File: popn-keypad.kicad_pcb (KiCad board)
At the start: 2 copper layers, 10 parts, among them U1 Arduino_Pro_Micro

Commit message: Defined edge cuts, added filled zones
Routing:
- added copper zone on B.Cu, net (none)
- added copper zone on F.Cu, net (none)
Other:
- board outline added: 123.8 x 38.1 mm
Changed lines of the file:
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@@
 		)
+	)
+	(gr_rect
+		(start 95.2 66.64)
+		(end 218.96 104.72)
+		(stroke
+			(width 0.05)
+			(type default)
+		)
+		(fill no)
+		(layer "Edge.Cuts")
 	)
 	(segment
@@
 		(net 10)
 	)
+	(zone
+		(net 0)
+		(net_name "")
+		(layers "F.Cu" "B.Cu")
+		(hatch edge 0.5)
+		(connect_pads
+			(clearance 0.5)
+		)
+		(min_thickness 0.25)
+		(filled_areas_thickness no)
+		(fill yes
+			(thermal_gap 0.5)
+			(thermal_bridge_width 0.5)
+			(island_removal_mode 1)
+			(island_area_min 10)
+		)
+		(polygon
+			(pts
+				(xy 85.68 57.12) (xy 228.48 57.12) (xy 228.48 114.24) (xy 85.68 114.24)
+			)
+		)
+	)
 	(embedded_fonts no)

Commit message: Hotfix
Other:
- board size 123.8 x 38.1 mm -> 119 x 42.8 mm
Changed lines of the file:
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@@
 	)
 	(gr_rect
-		(start 95.2 66.64)
+		(start 99.96 61.88)
 		(end 218.96 104.72)
 		(stroke

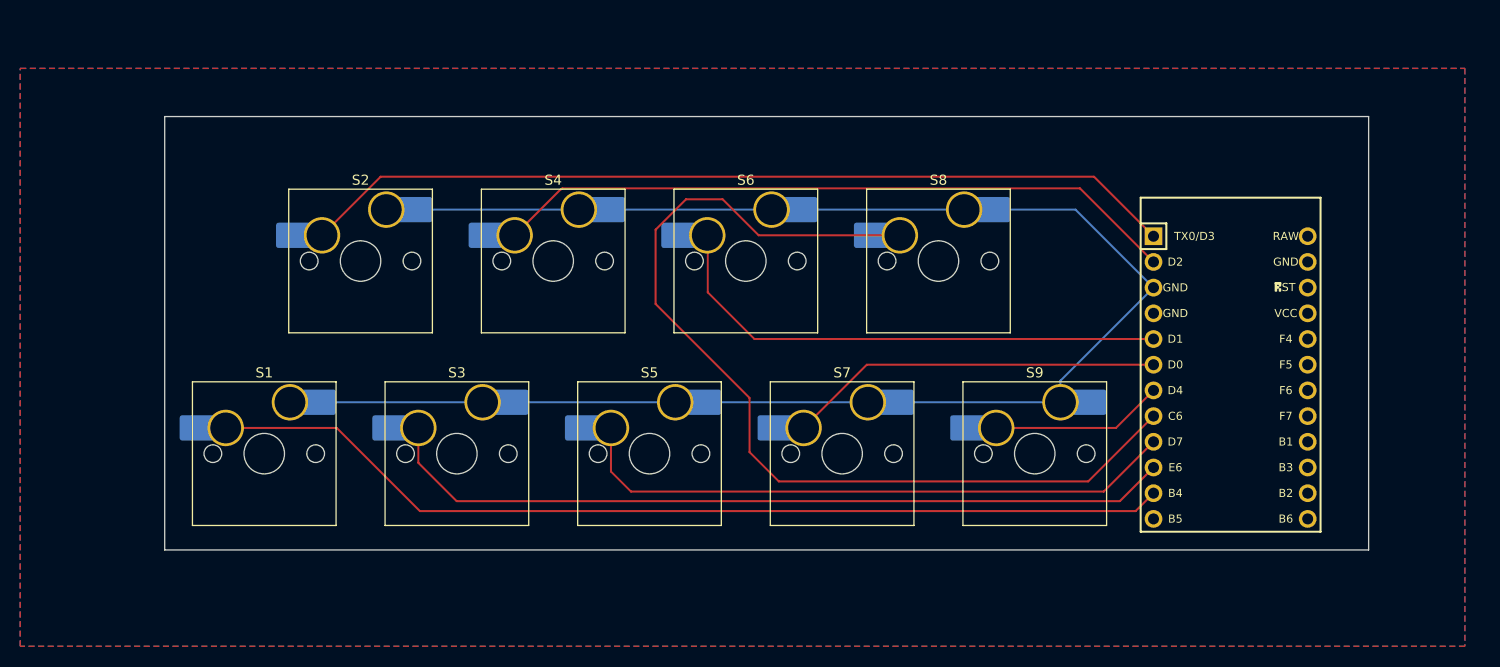
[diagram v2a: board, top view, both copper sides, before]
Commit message: Update popn-keypad.kicad_pcb
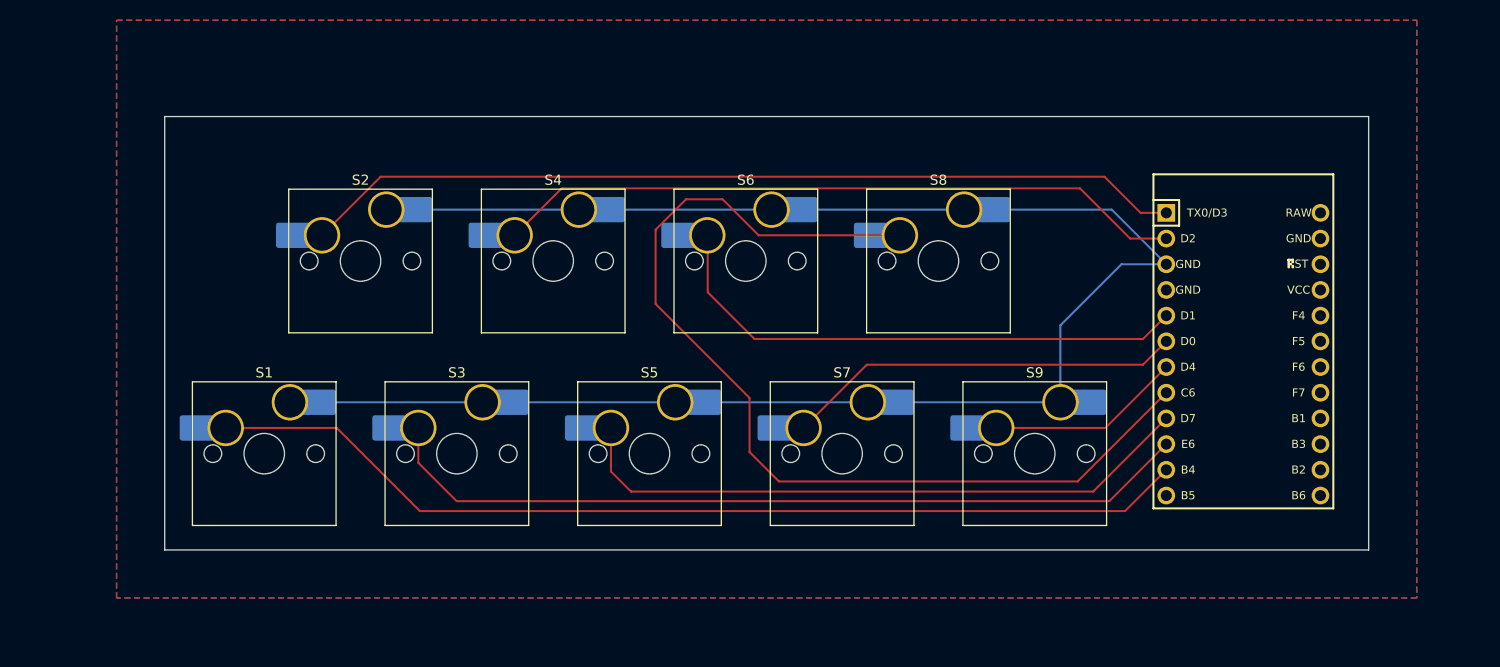
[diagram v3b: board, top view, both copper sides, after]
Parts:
- moved U1 2.63 mm to (206.6, 85.4)
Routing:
- net GND: track 170.3 -> 176.1 mm
- net S6: track 96.5 -> 98.7 mm
- net S7: track 60.8 -> 63.0 mm
- net S9: track 95.8 -> 98.1 mm
- net S8: track 79.1 -> 81.3 mm
- net S4: track 37.2 -> 39.4 mm
- net S3: track 51.6 -> 53.8 mm
- net S5: track 17.1 -> 19.3 mm
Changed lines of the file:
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@@
 	(footprint "ScottoKeebs_MCU:Arduino_Pro_Micro"
 		(layer "F.Cu")
-		(at 205.316987 87.679309)
+		(at 206.58 85.37)
 		(property "Reference" "U1"
 			(at 0 1.625 0)
@@
 	)
 	(segment
-		(start 189.987678 71.08)
-		(end 197.696987 78.789309)
+		(start 121.86 71.08)
+		(end 193.56 71.08)
 		(width 0.2)
 		(layer "B.Cu")
@@
 	)
 	(segment
-		(start 121.86 71.08)
-		(end 189.987678 71.08)
+		(start 188.5 82.5)
+		(end 188.5 90.12)
 		(width 0.2)
 		(layer "B.Cu")
@@
 	)
 	(segment
-		(start 188.5 87.986296)
-		(end 197.696987 78.789309)
+		(start 193.56 71.08)
+		(end 198.96 76.48)
 		(width 0.2)
 		(layer "B.Cu")
@@
 	)
 	(segment
-		(start 188.5 90.12)
-		(end 188.5 87.986296)
+		(start 198.96 76.48)
+		(end 194.52 76.48)
 		(width 0.2)
 		(layer "B.Cu")
@@
 	)
 	(segment
+		(start 194.52 76.48)
+		(end 188.5 82.5)
+		(width 0.2)
+		(layer "B.Cu")
+		(net 1)
+	)
+	(segment
 		(start 121.305071 67.824929)
-		(end 191.812607 67.824929)
+		(end 192.847942 67.824929)
 		(width 0.2)
 		(layer "F.Cu")
@@
 	)
 	(segment
-		(start 197.469309 73.709309)
-		(end 197.696987 73.709309)
+		(start 115.51 73.62)
+		(end 121.305071 67.824929)
 		(width 0.2)
 		(layer "F.Cu")
@@
 	)
 	(segment
-		(start 191.812607 67.824929)
-		(end 197.696987 73.709309)
+		(start 196.423013 71.4)
+		(end 198.96 71.4)
 		(width 0.2)
 		(layer "F.Cu")
@@
 	)
 	(segment
-		(start 115.51 73.62)
-		(end 121.305071 67.824929)
+		(start 192.847942 67.824929)
+		(end 196.423013 71.4)
 		(width 0.2)
 		(layer "F.Cu")
@@
 	)
 	(segment
-		(start 153.59 73.62)
-		(end 153.638407 73.668407)
+		(start 153.638407 79.254256)
+		(end 158.25346 83.869309)
+		(width 0.2)
+		(layer "F.Cu")
+		(net 3)
+	)
+	(segment
+		(start 153.638407 73.668407)
+		(end 153.638407 79.254256)
 		(width 0.2)
 		(layer "F.Cu")
@@
 	(segment
 		(start 158.25346 83.869309)
-		(end 197.696987 83.869309)
+		(end 196.650691 83.869309)
 		(width 0.2)
 		(layer "F.Cu")
@@
 	)
 	(segment
-		(start 153.638407 73.668407)
-		(end 153.638407 79.254256)
+		(start 196.650691 83.869309)
+		(end 198.96 81.56)
 		(width 0.2)
 		(layer "F.Cu")
@@
 	)
 	(segment
-		(start 153.638407 79.254256)
-		(end 158.25346 83.869309)
+		(start 153.59 73.62)
+		(end 153.638407 73.668407)
 		(width 0.2)
 		(layer "F.Cu")
@@
 	(segment
 		(start 182.15 92.66)
-		(end 193.986296 92.66)
+		(end 192.94 92.66)
 		(width 0.2)
 		(layer "F.Cu")
@@
 	)
 	(segment
-		(start 193.986296 92.66)
-		(end 197.696987 88.949309)
+		(start 192.94 92.66)
+		(end 198.96 86.64)
 		(width 0.2)
 		(layer "F.Cu")
@@
 	)
 	(segment
-		(start 146.048313 98.94635)
-		(end 192.779946 98.94635)
+		(start 191.73365 98.94635)
+		(end 198.96 91.72)
 		(width 0.2)
 		(layer "F.Cu")
@@
 	)
 	(segment
-		(start 144.07 96.968037)
-		(end 146.048313 98.94635)
+		(start 146.048313 98.94635)
+		(end 191.73365 98.94635)
 		(width 0.2)
 		(layer "F.Cu")
@@
 	)
 	(segment
-		(start 192.779946 98.94635)
-		(end 197.696987 94.029309)
+		(start 144.07 96.968037)
+		(end 146.048313 98.94635)
 		(width 0.2)
 		(layer "F.Cu")
@@
 	)
 	(segment
-		(start 195.929942 100.876354)
-		(end 197.696987 99.109309)
+		(start 116.966305 92.66)
+		(end 125.182659 100.876354)
 		(width 0.2)
 		(layer "F.Cu")
@@
 	)
 	(segment
-		(start 125.182659 100.876354)
-		(end 195.929942 100.876354)
+		(start 105.99 92.66)
+		(end 116.966305 92.66)
 		(width 0.2)
 		(layer "F.Cu")
@@
 	)
 	(segment
-		(start 116.966305 92.66)
-		(end 125.182659 100.876354)
+		(start 194.883646 100.876354)
+		(end 198.96 96.8)
 		(width 0.2)
 		(layer "F.Cu")
@@
 	)
 	(segment
-		(start 105.99 92.66)
-		(end 116.966305 92.66)
+		(start 125.182659 100.876354)
+		(end 194.883646 100.876354)
 		(width 0.2)
 		(layer "F.Cu")
@@
 	)
 	(segment
-		(start 190.426678 68.979)
-		(end 197.696987 76.249309)
+		(start 134.55 73.62)
+		(end 139.107368 69.062632)
 		(width 0.2)
 		(layer "F.Cu")
@@
 	)
 	(segment
-		(start 139.263362 68.979)
-		(end 190.426678 68.979)
+		(start 195.387678 73.94)
+		(end 198.96 73.94)
+		(width 0.2)
+		(layer "F.Cu")
+		(net 7)
+	)
+	(segment
+		(start 139.17973 69.062632)
+		(end 139.263362 68.979)
+		(width 0.2)
+		(layer "F.Cu")
+		(net 7)
+	)
+	(segment
+		(start 190.426678 68.979)
+		(end 195.387678 73.94)
 		(width 0.2)
 		(layer "F.Cu")
@@
 	)
 	(segment
-		(start 134.55 73.62)
-		(end 139.107368 69.062632)
+		(start 139.263362 68.979)
+		(end 190.426678 68.979)
 		(width 0.2)
 		(layer "F.Cu")
@@
 	)
 	(segment
-		(start 139.17973 69.062632)
-		(end 139.263362 68.979)
+		(start 169.360691 86.409309)
+		(end 196.650691 86.409309)
 		(width 0.2)
 		(layer "F.Cu")
-		(net 7)
+		(net 8)
 	)
 	(segment
@@
 	)
 	(segment
-		(start 169.360691 86.409309)
-		(end 197.696987 86.409309)
+		(start 196.650691 86.409309)
+		(end 198.96 84.1)
 		(width 0.2)
 		(layer "F.Cu")
@@
 	)
 	(segment
-		(start 155.103652 70.053563)
-		(end 151.493492 70.053563)
+		(start 158.670089 73.62)
+		(end 155.103652 70.053563)
 		(width 0.2)
 		(layer "F.Cu")
@@
 	)
 	(segment
-		(start 151.493492 70.053563)
-		(end 148.481312 73.065743)
+		(start 155.103652 70.053563)
+		(end 151.493492 70.053563)
 		(width 0.2)
 		(layer "F.Cu")
@@
 	)
 	(segment
-		(start 158.670089 73.62)
-		(end 155.103652 70.053563)
+		(start 190.195387 97.944613)
+		(end 198.96 89.18)
 		(width 0.2)
 		(layer "F.Cu")
@@
 	)
 	(segment
-		(start 148.481312 80.407018)
-		(end 157.764082 89.689788)
+		(start 148.481312 73.065743)
+		(end 148.481312 80.407018)
 		(width 0.2)
 		(layer "F.Cu")
@@
 	)
 	(segment
-		(start 160.664601 97.944613)
-		(end 191.241683 97.944613)
+		(start 172.63 73.62)
+		(end 158.670089 73.62)
 		(width 0.2)
 		(layer "F.Cu")
@@
 	)
 	(segment
-		(start 157.764082 89.689788)
-		(end 157.764082 95.044094)
+		(start 151.493492 70.053563)
+		(end 148.481312 73.065743)
 		(width 0.2)
 		(layer "F.Cu")
@@
 	)
 	(segment
-		(start 172.63 73.62)
-		(end 158.670089 73.62)
+		(start 160.664601 97.944613)
+		(end 190.195387 97.944613)
 		(width 0.2)
 		(layer "F.Cu")
@@
 	)
 	(segment
-		(start 148.481312 73.065743)
-		(end 148.481312 80.407018)
+		(start 148.481312 80.407018)
+		(end 157.764082 89.689788)
 		(width 0.2)
 		(layer "F.Cu")
@@
 	)
 	(segment
-		(start 191.241683 97.944613)
-		(end 197.696987 91.489309)
+		(start 157.764082 89.689788)
+		(end 157.764082 95.044094)
 		(width 0.2)
 		(layer "F.Cu")
@@
 	(segment
 		(start 128.820296 99.893447)
-		(end 194.372849 99.893447)
+		(end 193.326553 99.893447)
 		(width 0.2)
 		(layer "F.Cu")
@@
 	)
 	(segment
-		(start 194.372849 99.893447)
-		(end 197.696987 96.569309)
+		(start 193.326553 99.893447)
+		(end 198.96 94.26)
 		(width 0.2)
 		(layer "F.Cu")
@@
 		(polygon
 			(pts
-				(xy 85.68 57.12) (xy 228.48 57.12) (xy 228.48 114.24) (xy 85.68 114.24)
+				(xy 223.72 52.36) (xy 223.72 109.48) (xy 95.2 109.48) (xy 95.2 52.36)
 			)
 		)

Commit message: Major rewiring
I got rid of all of my ground lines in favor of a copper fill connected to ground. This made the routing my traces far less convoluted.
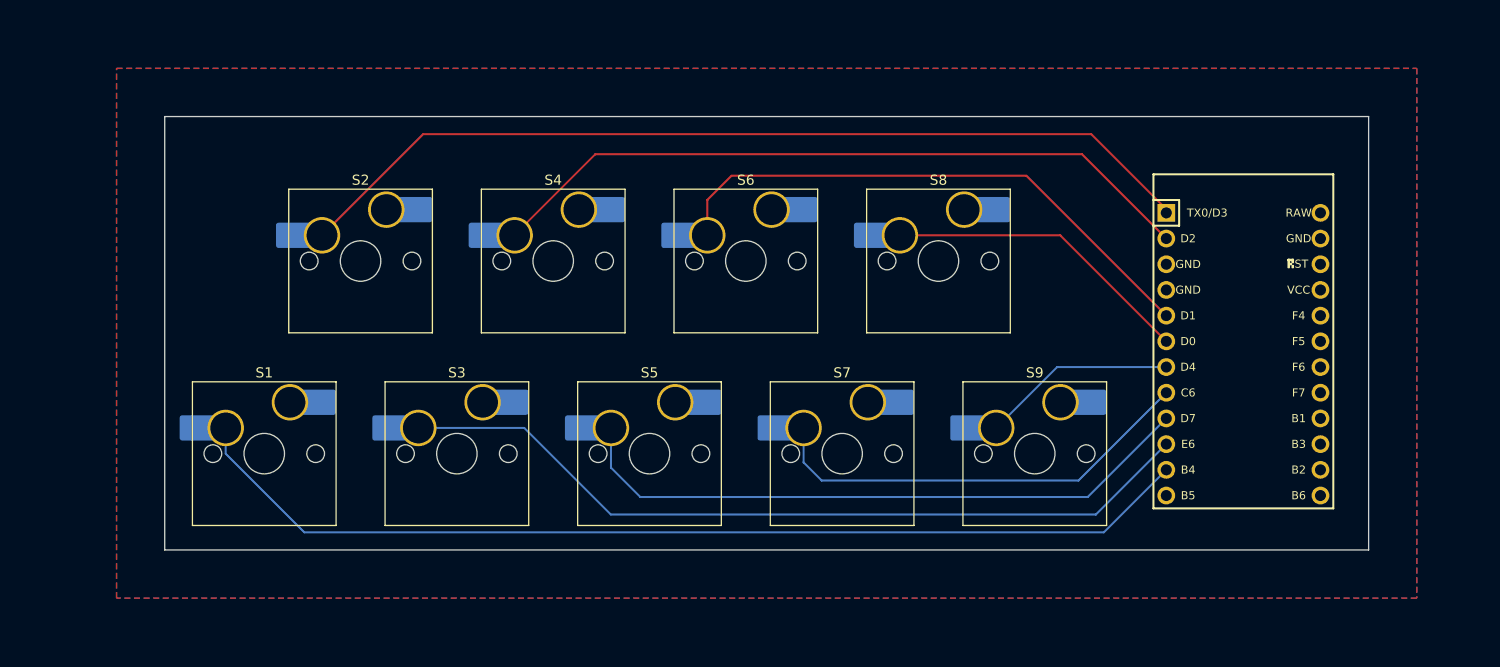
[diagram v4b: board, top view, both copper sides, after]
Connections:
- S7 pad 1: S4 -> S6
- S8 pad 1: S6 -> S4
- U1 pad 4: unconnected-(U1-GND-Pad4) -> GND
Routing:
- net GND: track 176.1 -> 0.00 mm
- net S6: track 98.7 -> 43.6 mm
- net S4: track 39.4 -> 30.7 mm
- net S1: track 87.3 -> 91.0 mm
- net S9: track 98.1 -> 101.3 mm
- net S2: track 68.4 -> 71.2 mm
- net S3: track 53.8 -> 55.7 mm
- net S8: track 81.3 -> 80.4 mm
- added copper zone on B.Cu, net GND
- added copper zone on F.Cu, net GND
- removed copper zone on B.Cu, net (none)
- removed copper zone on F.Cu, net (none)

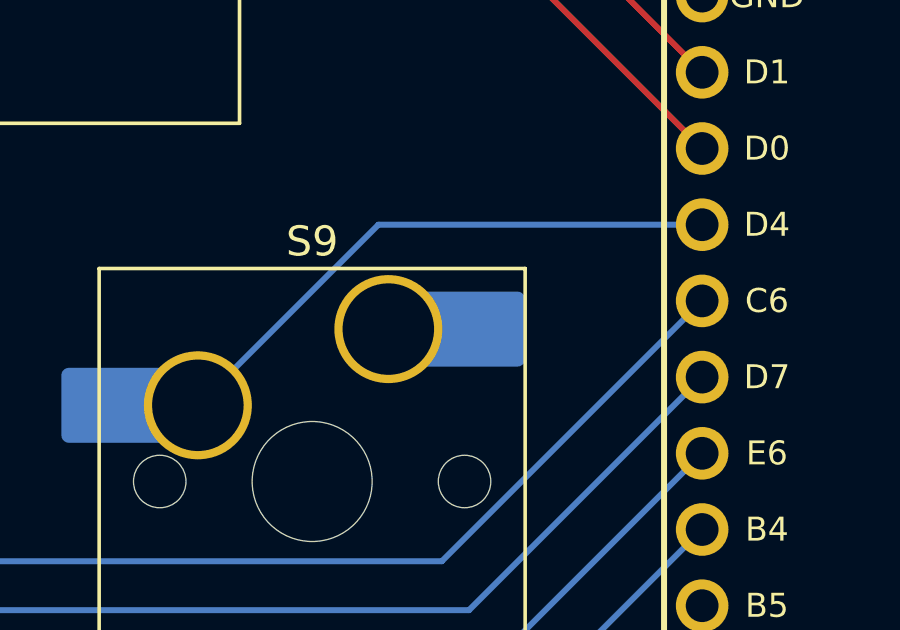
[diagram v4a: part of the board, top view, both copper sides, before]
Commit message: Fixed error
Fixed "Thermal relief connection to zone incomplete" error on the ground pin on S9.
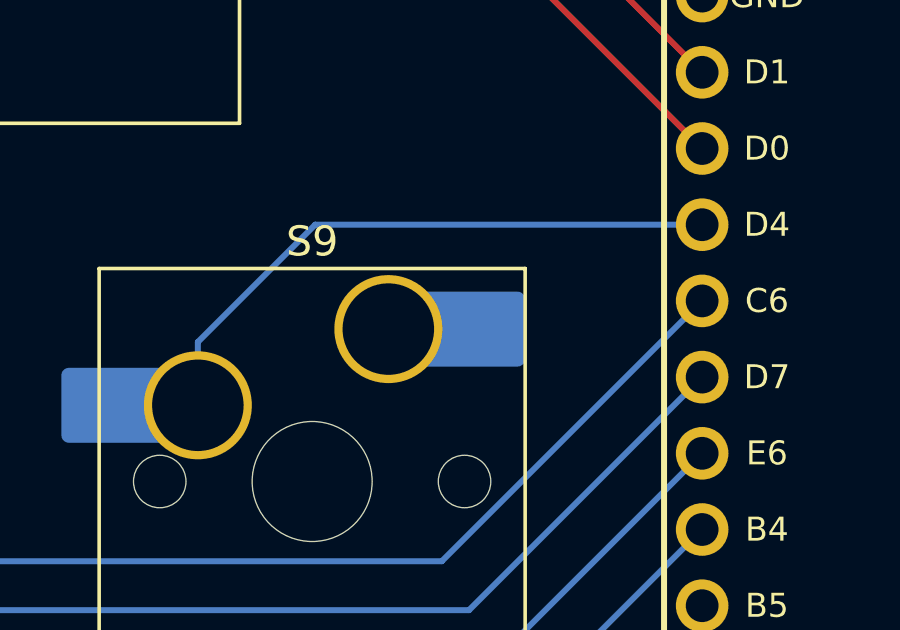
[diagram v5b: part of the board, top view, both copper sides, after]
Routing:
- net S5: track 19.3 -> 20.5 mm
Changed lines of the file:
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@@
 	)
 	(segment
-		(start 188.17 86.64)
-		(end 198.96 86.64)
+		(start 182.15 90.55099)
+		(end 186.06099 86.64)
 		(width 0.2)
 		(layer "B.Cu")
@@
 	(segment
 		(start 182.15 92.66)
-		(end 188.17 86.64)
+		(end 182.15 90.55099)
 		(width 0.2)
 		(layer "B.Cu")
+		(net 4)
+	)
+	(segment
+		(start 186.06099 86.64)
+		(end 198.96 86.64)
+		(width 0.2)
+		(layer "B.Cu")

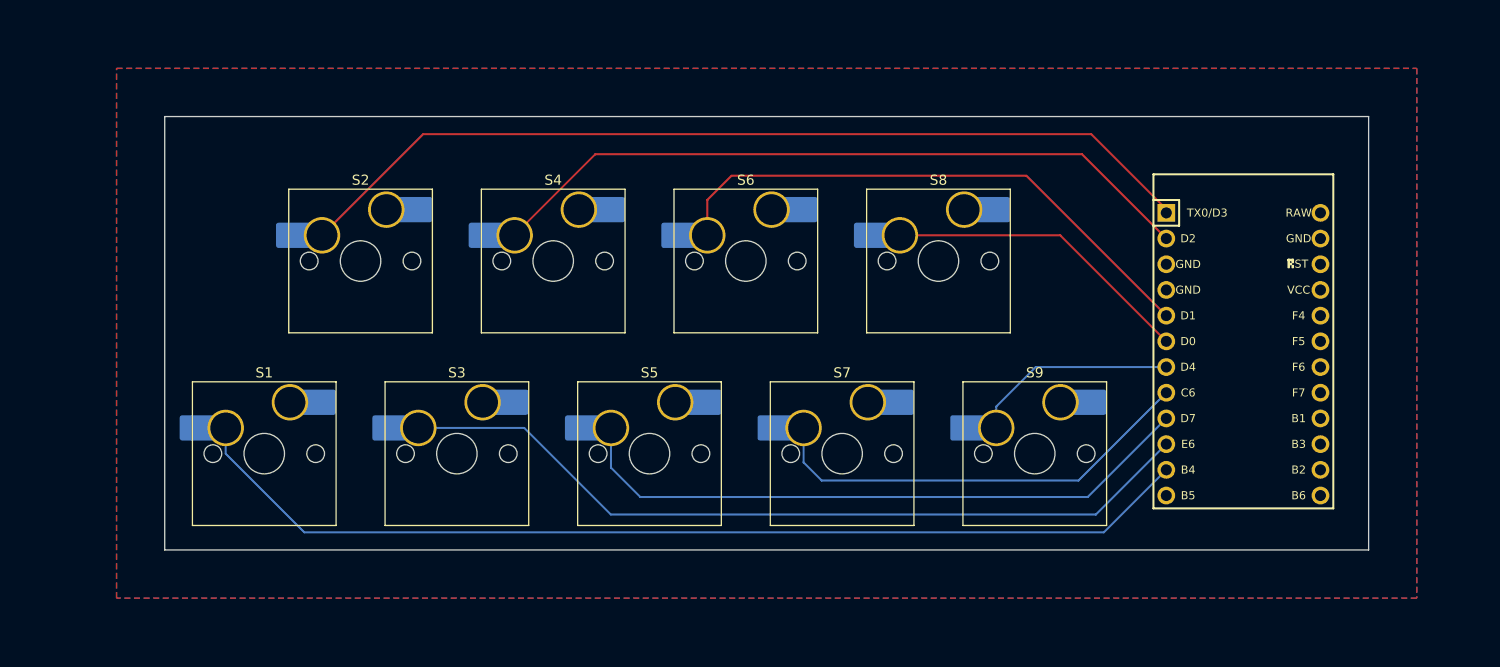
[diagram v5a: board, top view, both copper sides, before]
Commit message: Added mounting holes, adjusted dimensions
Added M2 mounting holes to the board, reduced the height of it (adjusting the traces as needed). Rebuilt production files.
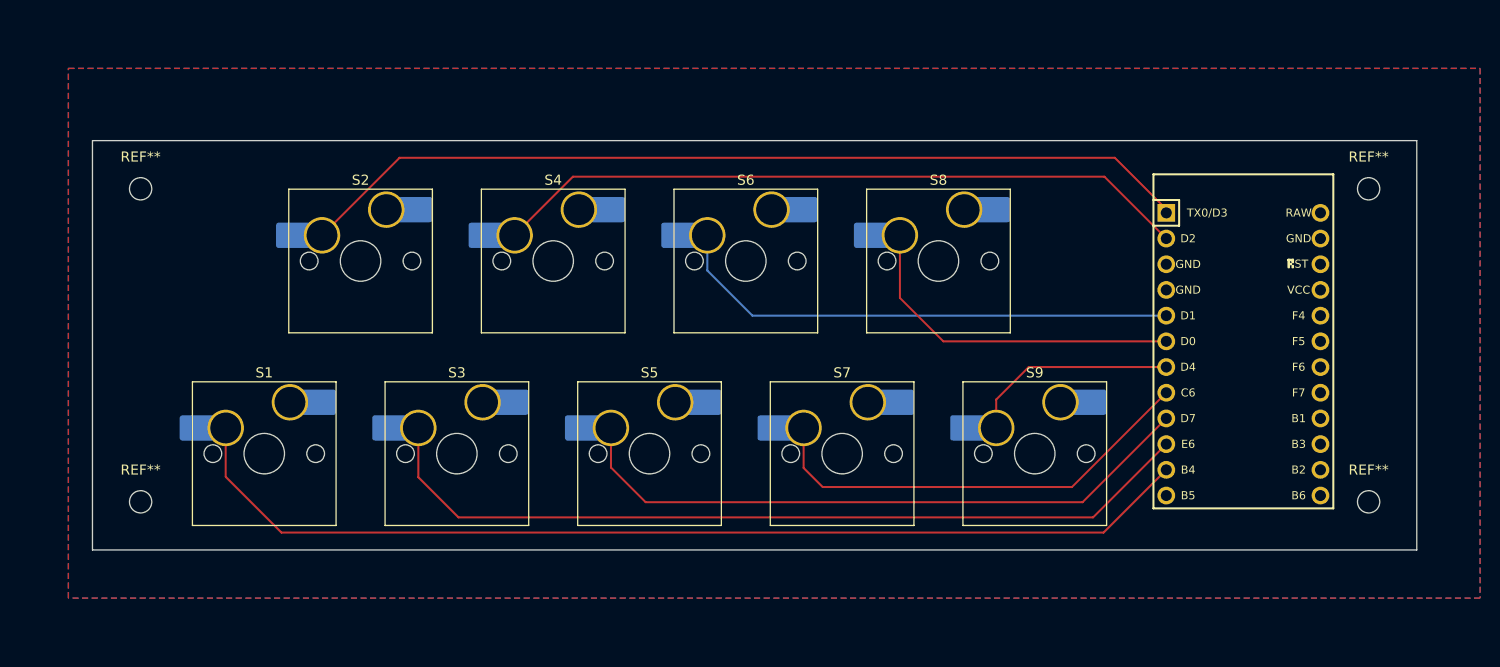
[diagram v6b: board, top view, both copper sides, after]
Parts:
- added REF**: MountingHole_2.2mm_M2, MountingHole:MountingHole_2.2mm_M2, F.Cu at (97.6, 100.0)
- added REF**: MountingHole_2.2mm_M2, MountingHole:MountingHole_2.2mm_M2, F.Cu at (219.0, 69.0)
- added REF**: MountingHole_2.2mm_M2, MountingHole:MountingHole_2.2mm_M2, F.Cu at (219.0, 100.0)
- added REF**: MountingHole_2.2mm_M2, MountingHole:MountingHole_2.2mm_M2, F.Cu at (97.6, 69.0)
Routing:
- net S3: track 55.7 -> 50.8 mm
- net S4: track 30.7 -> 34.3 mm
- net S8: track 80.4 -> 83.4 mm
- net S1: track 91.0 -> 89.1 mm
- net S2: track 71.2 -> 69.4 mm
- net S9: track 101.3 -> 102.7 mm
- net S6: track 43.6 -> 44.4 mm
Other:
- board size 119 x 42.8 mm -> 130.9 x 40.5 mm
